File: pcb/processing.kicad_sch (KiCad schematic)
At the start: 27 parts, among them IC4 STM32F405RGT6TR, J2 503398-1892, SW1 SW_Push, U2 LMK6CE

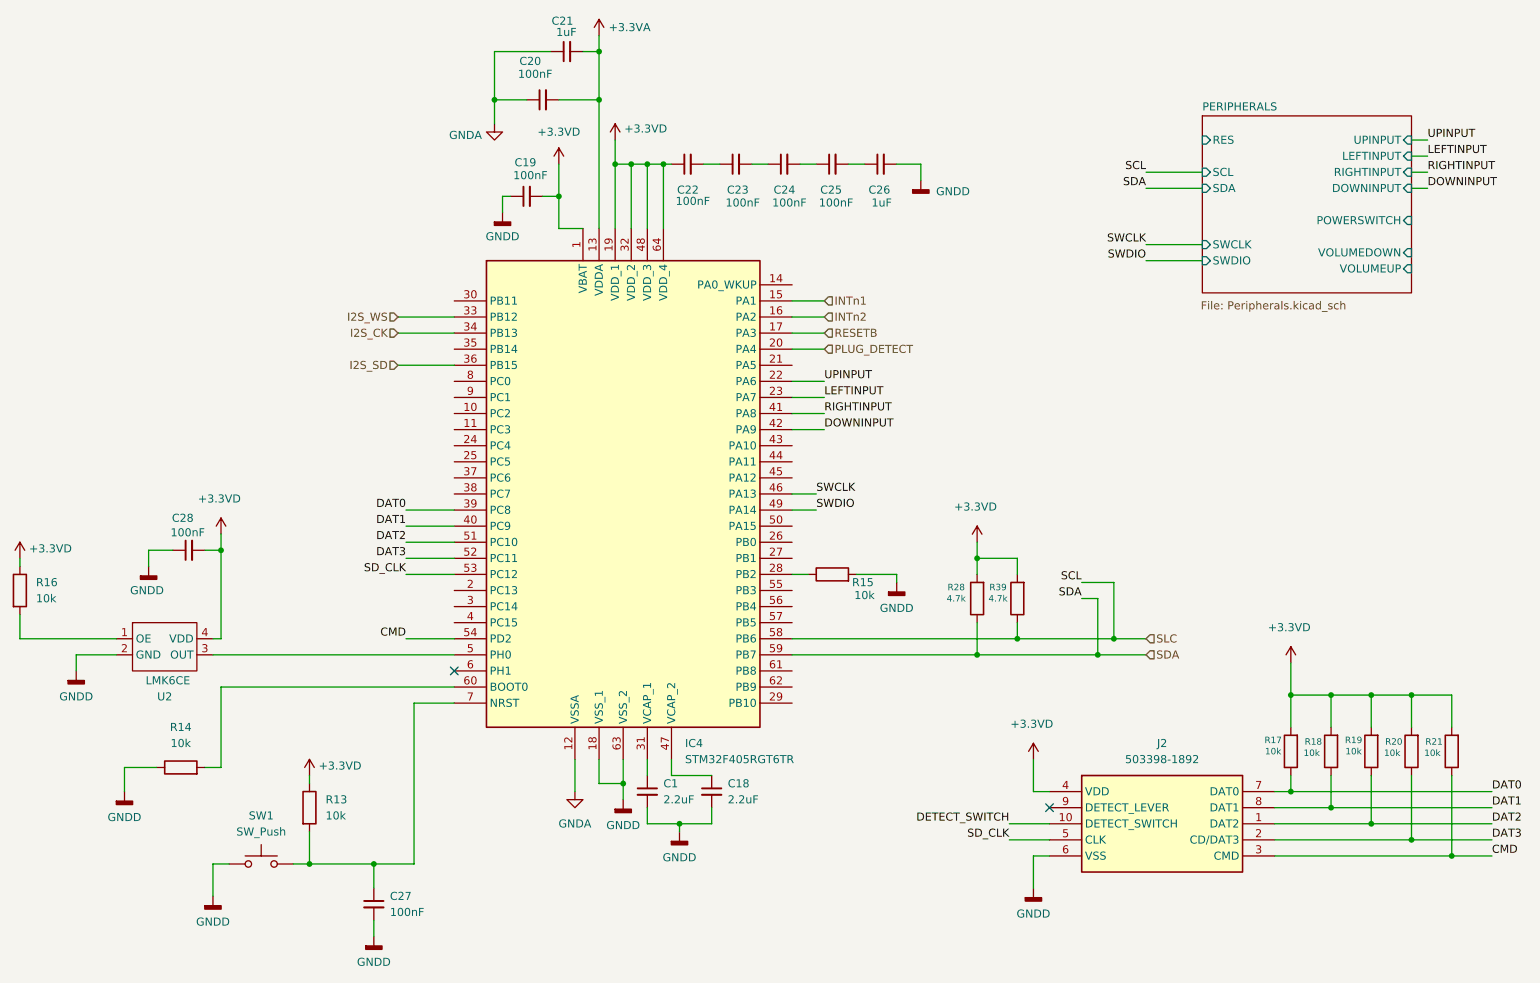
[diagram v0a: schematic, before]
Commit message: latest updates to schematic, changed to continuous ground
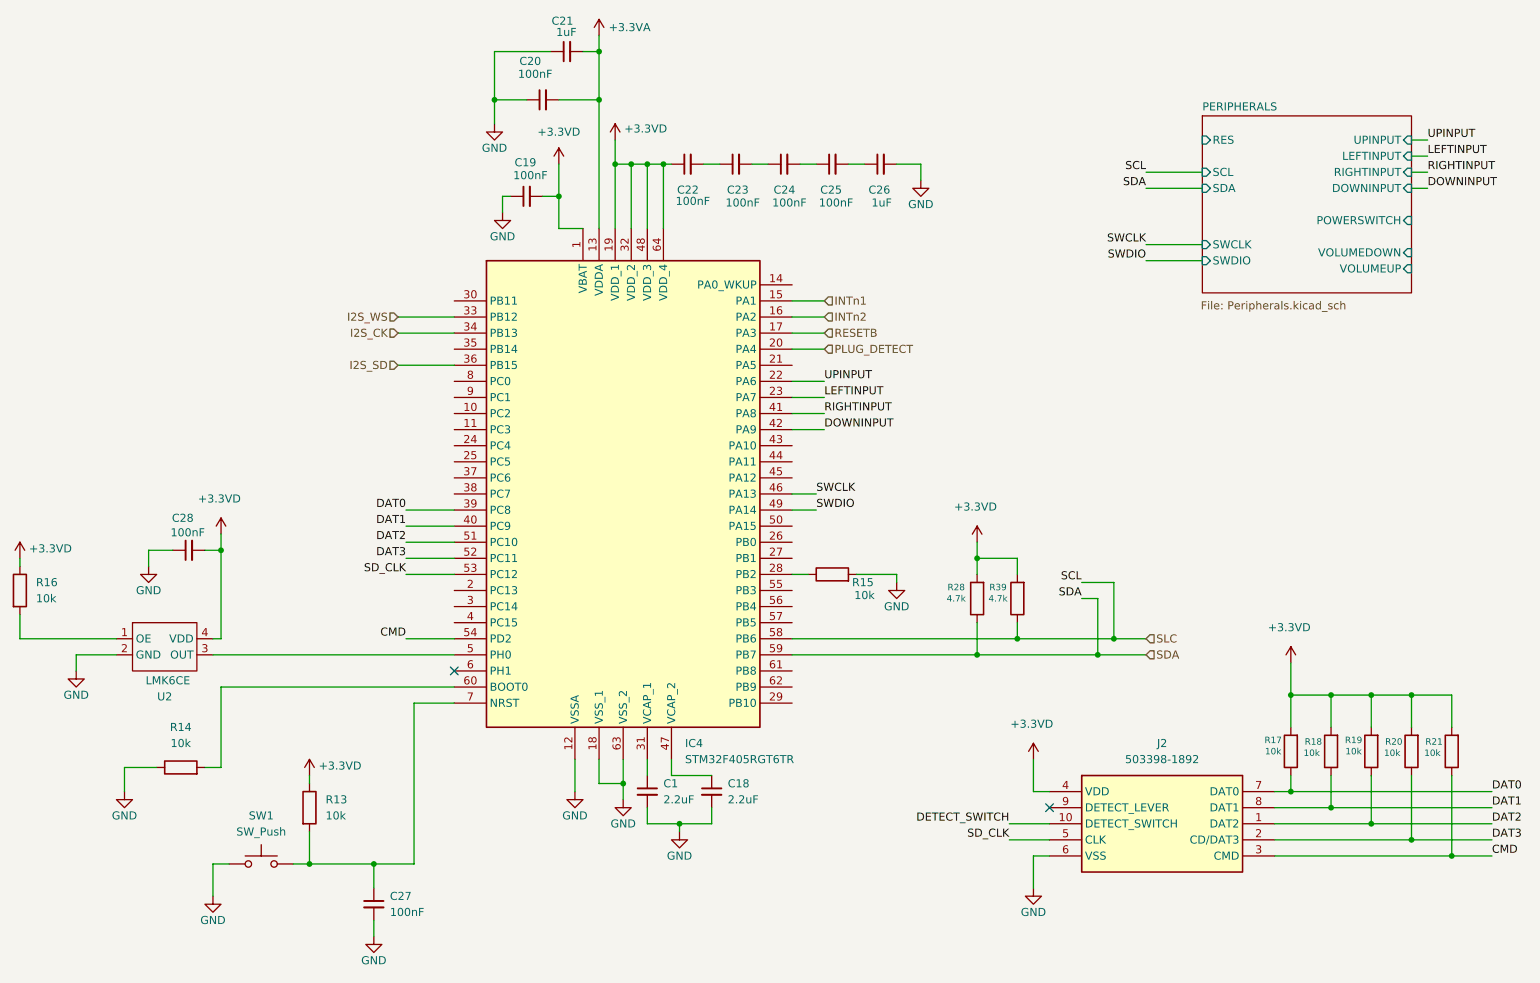
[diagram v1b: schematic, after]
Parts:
- C1, C18, C19, C20, C21, C22, C23, C24, C25, C26, C27, C28: footprint (none) -> Capacitor_SMD:C_0805_2012Metric
- IC4: footprint QFP50P1200X1200X160-64N -> STM32F405RGT6TR:QFP50P1200X1200X160-64N
- J2: footprint 5033981892 -> 503398-1892:5033981892
- R13, R14, R15, R16, R17, R18, R19, R20, R21, R28, R39: footprint (none) -> Resistor_SMD:R_0805_2012Metric
- SW1: footprint (none) -> Button_Switch_SMD:SW_Push_1P1T-MP_NO_Horizontal_Alps_SKRTLAE010
- U2: footprint (none) -> BAW:DLF0004A
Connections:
- net GNDD is gone; now on net GND: C1.2, C18.2, C19.1, C26.2, C27.2, C28.1, IC4.18 (VSS_1), IC4.63 (VSS_2), J2.6 (VSS), R14.1, R15.2, SW1.1, U2.2 (GND)
- net GNDA renamed GND
